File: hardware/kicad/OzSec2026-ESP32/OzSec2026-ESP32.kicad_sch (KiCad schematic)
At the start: 59 parts, among them J1 UART, J2 USB_C_Receptacle_USB2.0, J3 JTAG, J4 DISPLAY, J5 Conn_01x03_Socket, SW1 SW_Push, SW2 SW_Push, SW3 SW_Push, SW4 SW_Push, SW5 POWER, SW6 SW_Push, SW7 SW_Push, U1 USBLC6-2SC6, U2 ESP32-S3-WROOM-1, U3 ME4054BM5G-N, U4 TLV1117LV-33, U5 VSMY14940, X1 Simple_Addon_v2

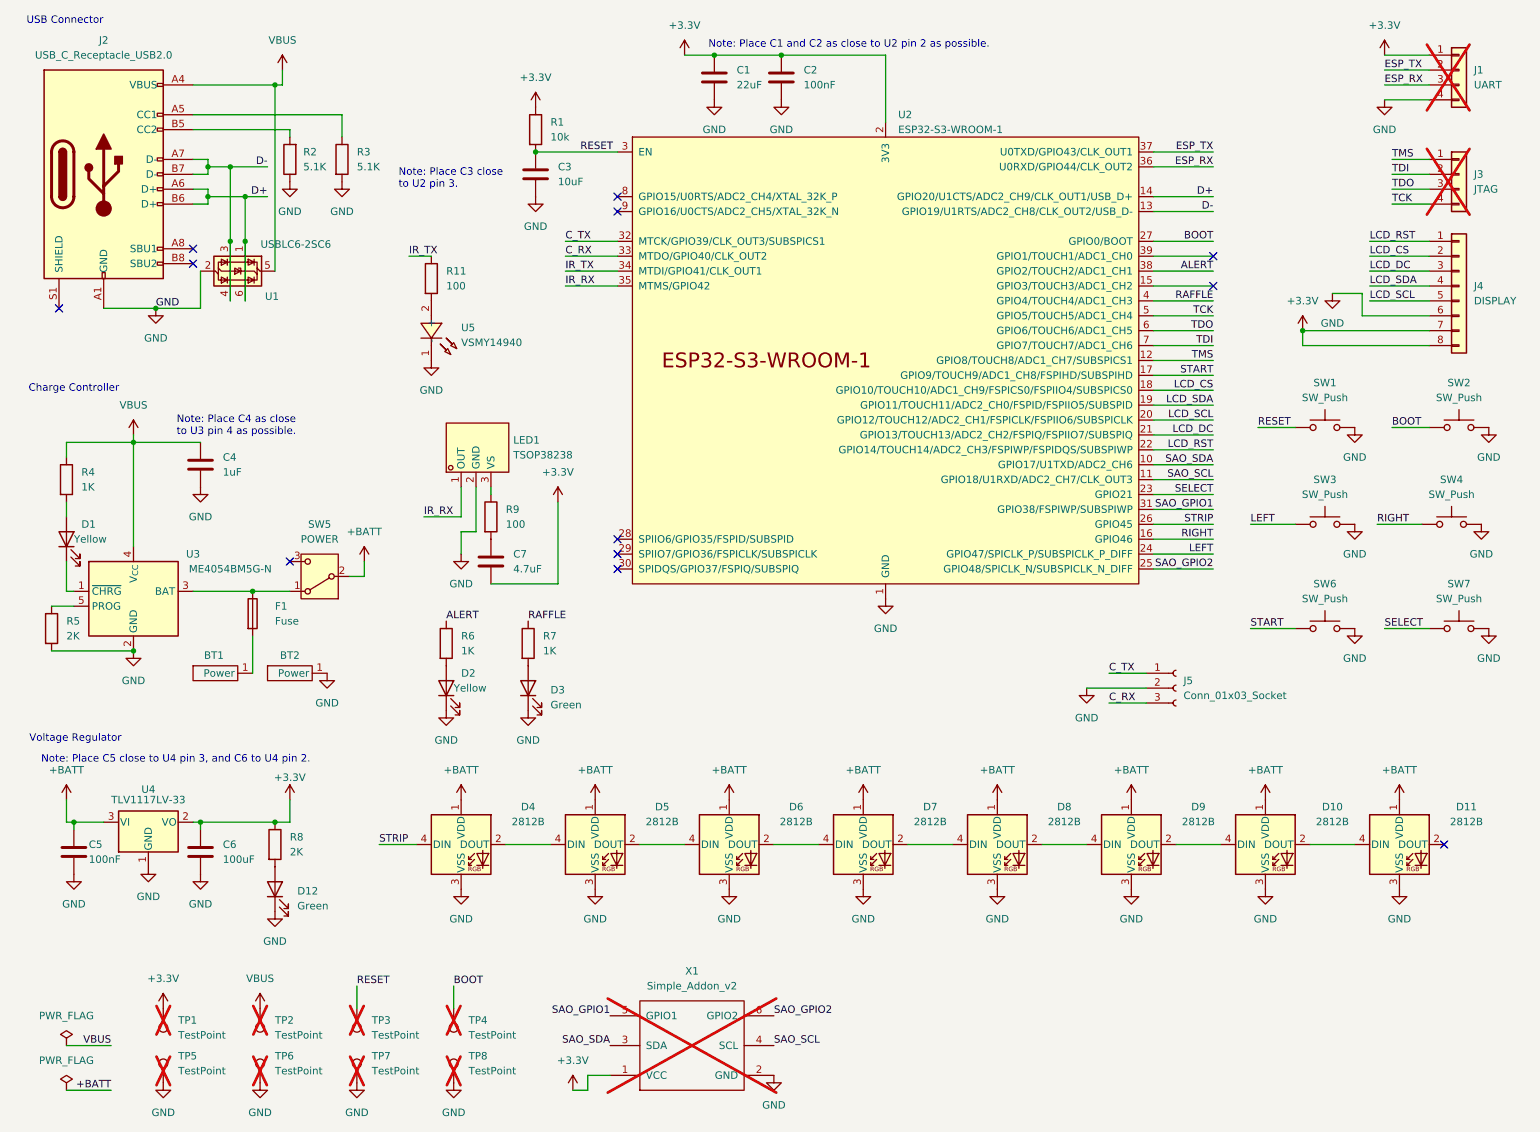
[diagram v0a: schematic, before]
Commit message: Fabrication files for prototype 1.
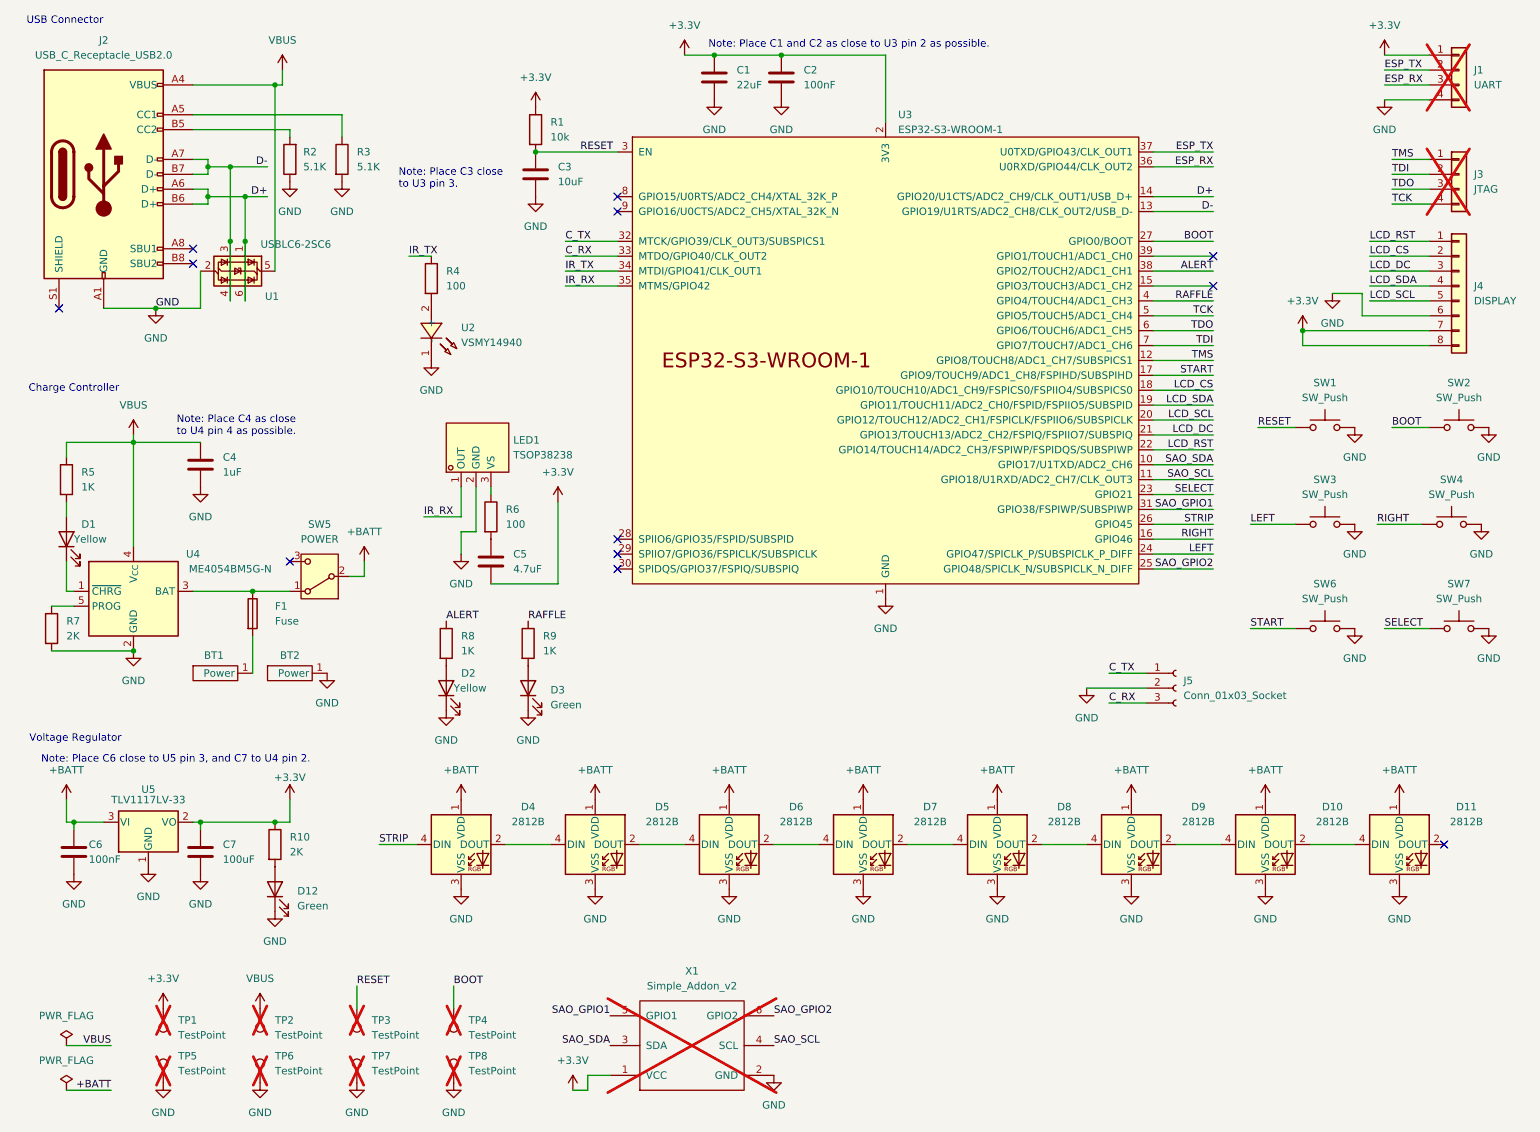
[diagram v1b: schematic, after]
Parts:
- renumbered C7 to C5, C5 to C6, C6 to C7, R8 to R10, R11 to R4, R4 to R5, R9 to R6, R5 to R7, R6 to R8, R7 to R9, U5 to U2, U2 to U3, U3 to U4, U4 to U5
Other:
- note added: "Note: Place C1 and C2 as close to U3 pin 2 as possible."
- note added: "Note: Place C3 close to U3 pin 3."
- note added: "Note: Place C4 as close to U4 pin 4 as possible."
- note added: "Note: Place C6 close to U5 pin 3, and C7 to U4 pin 2."
- note removed: "Note: Place C1 and C2 as close to U2 pin 2 as possible."
- note removed: "Note: Place C3 close to U2 pin 3."
- note removed: "Note: Place C4 as close to U3 pin 4 as possible."
- note removed: "Note: Place C5 close to U4 pin 3, and C6 to U4 pin 2."

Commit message: Version 1.1 of PCB and some initial source files.
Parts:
- BT1, BT2: LCSC (none) -> C2979179; Link (none) -> https://www.lcsc.com/product-detail/C2979179.html
- D1: renamed from U2; LCSC (none) -> C511069; LCSC Part C511069 -> (none); Link (none) -> https://www.lcsc.com/product-detail/C511069.html
- R10: value 2K -> 10K; LCSC C17604 -> C17414; Link https://www.lcsc.com/product-detail/C17604.html -> https://www.lcsc.com/product-detail/C17414.html
- SW1, SW2: LCSC (none) -> C318884; Link (none) -> https://www.lcsc.com/product-detail/C318884.html
- SW3, SW6, SW7: footprint ozsec-custom:SW_Push_1P1T_XKB_TS-1187A -> ozsec-custom:SW-SMD_4P-L4.5-W4.5-P3.00-LS6.8; LCSC (none) -> C2888900; Link (none) -> https://www.lcsc.com/product-detail/C2888900.html
- SW4: footprint ozsec-custom:SW_Push_1P1T_XKB_TS-1187A -> ozsec-custom:SW-SMD_4P-L4.5-W4.5-P3.00-LS6.8; LCSC (none) -> C2888900; Link (none) -> https://www.lcsc.com/product-detail/C2888900html
- U2: renamed from U3; Link (none) -> https://www.lcsc.com/product-detail/C2913201.html
- U3: renamed from LED1; LCSC (none) -> C141632; Link (none) -> https://www.lcsc.com/product-detail/C141632.html
- renumbered D9 to D10, D10 to D11, D11 to D12, D12 to D13, D1 to D2, D2 to D3, D3 to D4, D4 to D5, D5 to D6, D6 to D7, D7 to D8, D8 to D9
